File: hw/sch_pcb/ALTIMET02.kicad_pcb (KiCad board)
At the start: 2 copper layers, 40.1 x 19.8 mm, 14 parts, among them IC1 MS561101BA03-50, J2 HEADER_2x03, J3 HEADER_2x05_PARALLEL

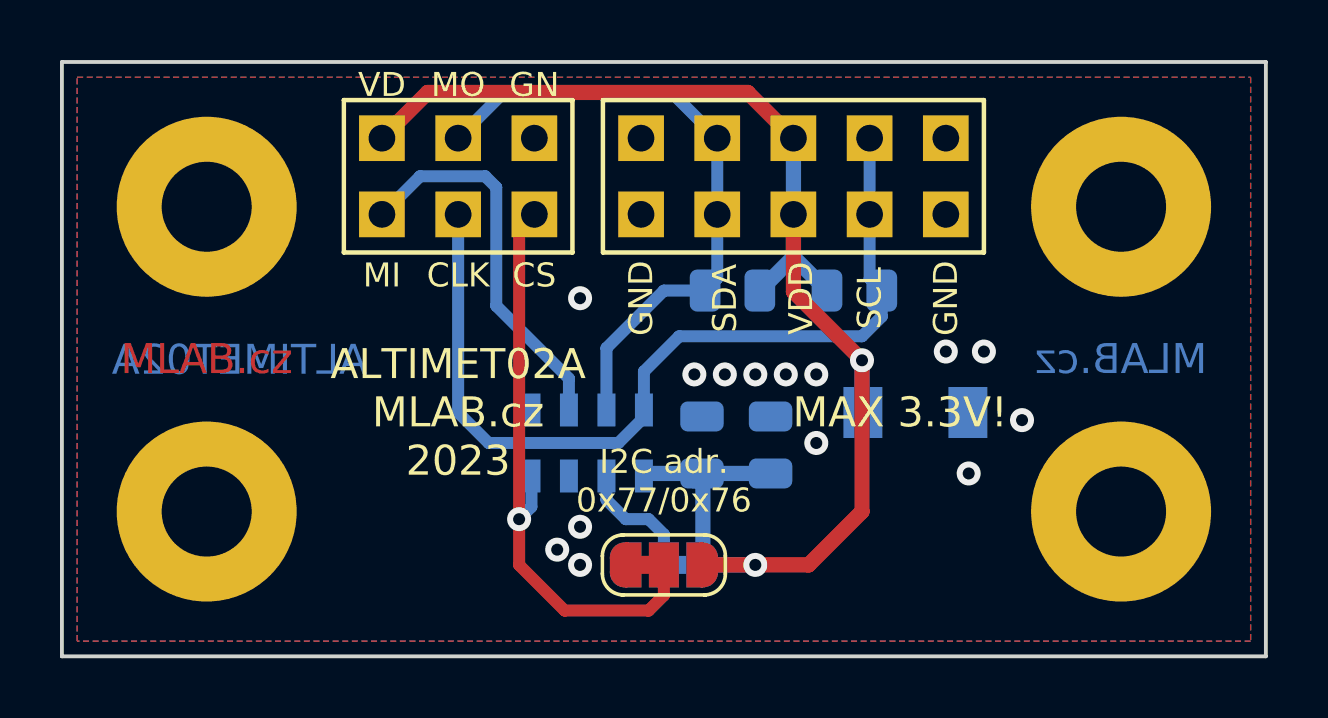
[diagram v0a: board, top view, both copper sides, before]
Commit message: power connector added, SPI and I2C connectors modified, default I2C adrress changed
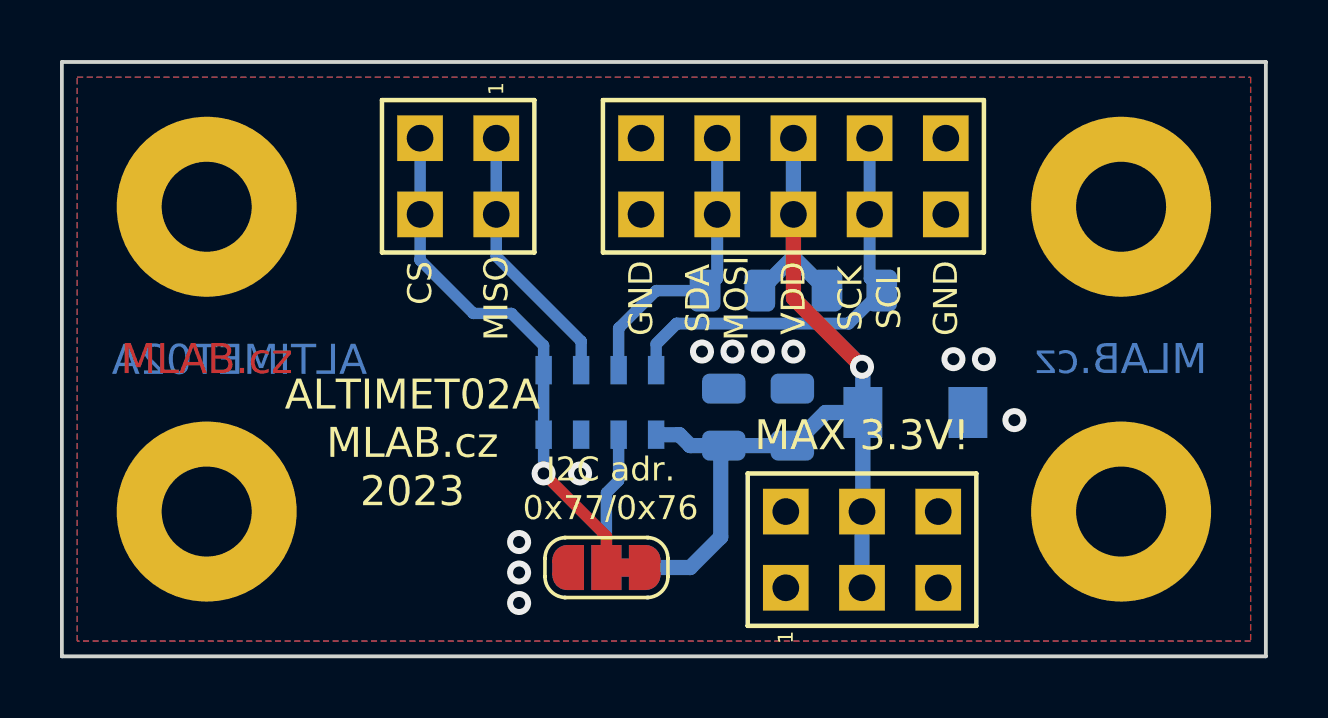
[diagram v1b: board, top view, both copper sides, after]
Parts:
- removed IC1: MS561101BA03-50, KiCad:MS561101BA03-50
- added J1: HEADER_2x02_PARALLEL, Mlab_Pin_Headers:Straight_2x02, F.Cu at (125.2, 100.6)
- added U1: MS5611-01BA, Package_LGA:LGA-8_3x5mm_P1.25mm, B.Cu at (129.9, 108.1)
- J2: value HEADER_2x03 -> HEADER_2x03_PARALLEL
- R1, R2: value DNF -> 5k
- moved J2 18.3 mm to (138.7, 113.0)
- moved JP1 1.92 mm to (130.2, 113.6)
- moved JP3 1.92 mm to (130.2, 113.6), turned to 180 degrees
- moved C1 1.18 mm to (134.1, 108.6)
- moved C2 1.18 mm to (136.4, 108.6)
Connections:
- J2 pad 1: MISO -> GND
- J2 pad 2: VDD -> GND
- J2 pad 3: SCLK -> VDD
- J2 pad 4: MOSI/SDA -> VDD
- J2 pad 5: CS/A -> GND
- JP3 pad 1: GND -> VDD
- JP3 pad 3: VDD -> GND
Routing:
- net VDD: track 50.4 -> 34.8 mm, vias 2 -> 1
- net SCLK: track 29.9 -> 14.4 mm
- net MOSI/SDA: track 21.3 -> 10.0 mm
- net MISO: track 13.4 -> 8.91 mm
- net CS/A: track 20.2 -> 17.6 mm
- net GND: vias 14 -> 11
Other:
- board text added: "MISO"
- board text added: "SCK SCL"
- board text added: "SDA MOSI"
- board text removed: "CLK"
- board text removed: "GN"
- board text removed: "MI"
- board text removed: "MO"
- board text removed: "SCL"
- board text removed: "SDA"
- board text removed: "VD"

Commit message: minor changes in layout, change diode
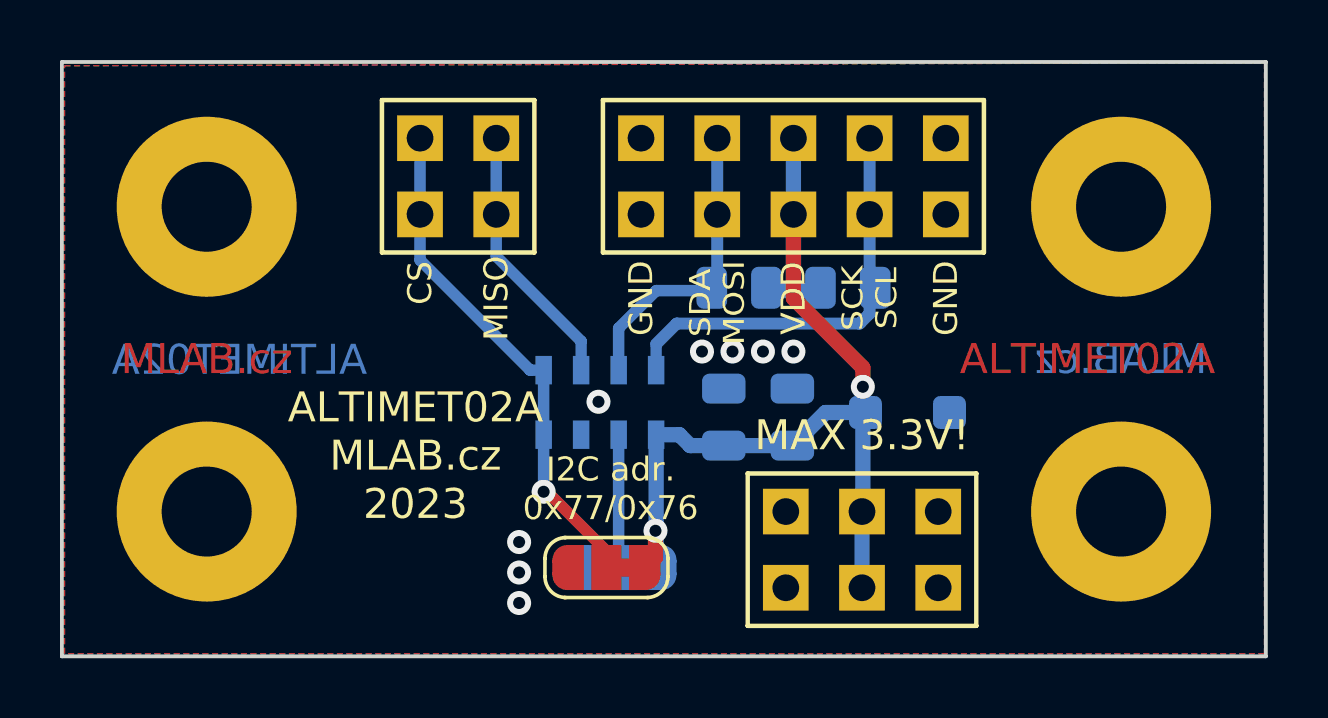
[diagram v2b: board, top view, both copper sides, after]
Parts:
- D1: value BZV55C3V6 -> BZT52H-C3V6,115; footprint Mlab_D:Diode-MiniMELF_Standard -> Diode_SMD:D_SOD-123F
- moved JP1 0.53 mm to (130.7, 113.6)
- moved D1 0.26 mm to (140.2, 108.5)
- moved R2 0.24 mm to (134.6, 104.3)
- moved R1 0.24 mm to (138.2, 104.3)
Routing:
- net VDD: vias 1 -> 2
- net GND: vias 11 -> 8

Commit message: add fiducial
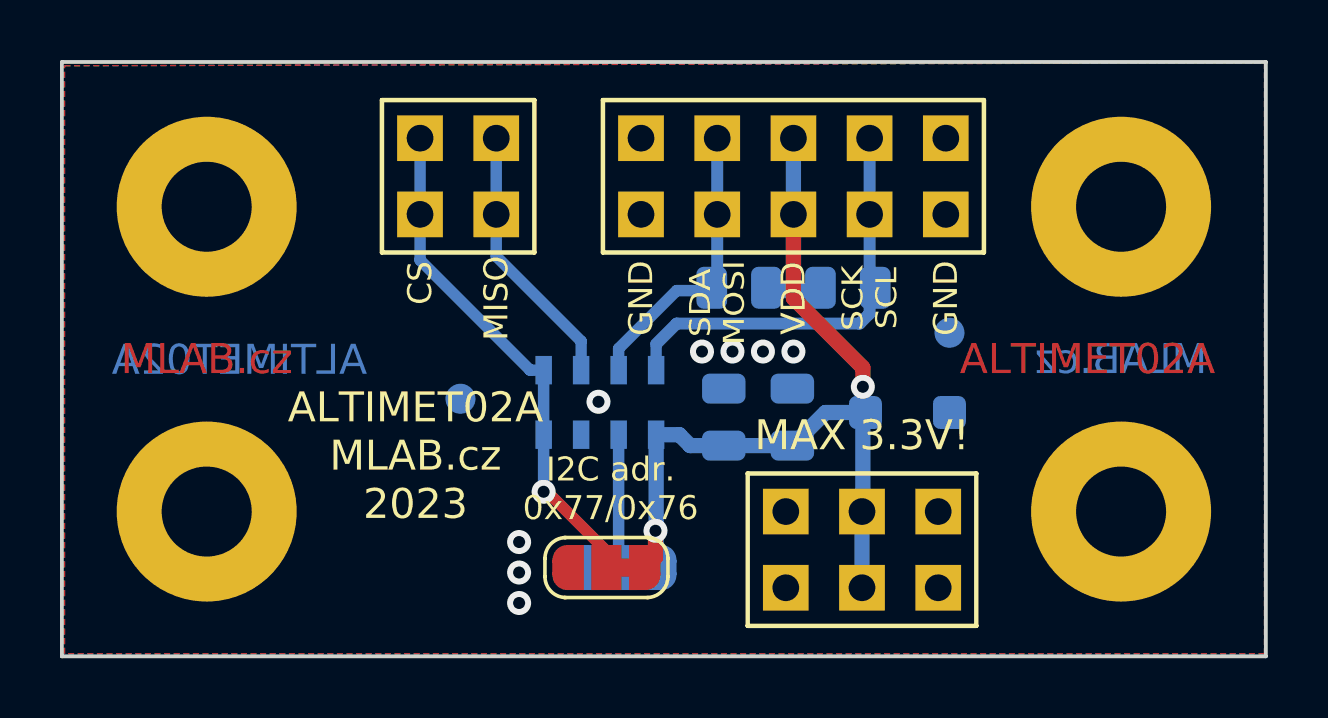
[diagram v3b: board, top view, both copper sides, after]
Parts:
- added FID1: Fiducial, Fiducial:Fiducial_1mm_Mask2mm, B.Cu at (141.6, 105.8)
- added FID2: Fiducial, Fiducial:Fiducial_1mm_Mask2mm, B.Cu at (125.3, 108.0)
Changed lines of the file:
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@@
     )
+  )
+  (footprint "Fiducial:Fiducial_1mm_Mask2mm" (layer "B.Cu")
+    (at 125.3 108 180)
+    (descr "Circular Fiducial, 1mm bare copper, 2mm soldermask opening (Level A)")
+    (tags "fiducial")
+    (property "Sheetfile" "ALTIMET02.kicad_sch")
+    (property "Sheetname" "")
+    (property "ki_description" "Fiducial Marker")
+    (property "ki_keywords" "fiducial marker")
+    (attr smd)
+    (fp_text reference "FID2" (at 0 2) (layer "B.SilkS") hide
+        (effects (font (size 1 1) (thickness 0.15)) (justify mirror))
+    )
+    (fp_text value "Fiducial" (at 0 -2) (layer "B.Fab")
+        (effects (font (size 1 1) (thickness 0.15)) (justify mirror))
+    )
+    (fp_text user "${REFERENCE}" (at 0 0) (layer "B.Fab")
+        (effects (font (size 0.4 0.4) (thickness 0.06)) (justify mirror))
+    )
+    (fp_circle (center 0 0) (end 1.25 0)
+      (stroke (width 0.05) (type solid)) (fill none) (layer "B.CrtYd"))
+    (fp_circle (center 0 0) (end 1 0)
+      (stroke (width 0.1) (type solid)) (fill none) (layer "B.Fab"))
+    (pad "" smd circle (at 0 0 180) (size 1 1) (layers "B.Cu" "B.Mask")
+      (solder_mask_margin 0.5) (clearance 0.5))
   )
   (footprint "Resistor_SMD:R_0805_2012Metric" (layer "B.Cu")
@@
       (rotate (xyz 0 0 0))
     )
+  )
+  (footprint "Fiducial:Fiducial_1mm_Mask2mm" (layer "B.Cu")
+    (at 141.6 105.8 180)
+    (descr "Circular Fiducial, 1mm bare copper, 2mm soldermask opening (Level A)")
+    (tags "fiducial")
+    (property "Sheetfile" "ALTIMET02.kicad_sch")
+    (property "Sheetname" "")
+    (property "ki_description" "Fiducial Marker")
+    (property "ki_keywords" "fiducial marker")
+    (attr smd)
+    (fp_text reference "FID1" (at 0 2) (layer "B.SilkS") hide
+        (effects (font (size 1 1) (thickness 0.15)) (justify mirror))
+    )
+    (fp_text value "Fiducial" (at 0 -2) (layer "B.Fab")
+        (effects (font (size 1 1) (thickness 0.15)) (justify mirror))
+    )
+    (fp_text user "${REFERENCE}" (at 0 0) (layer "B.Fab")
+        (effects (font (size 0.4 0.4) (thickness 0.06)) (justify mirror))
+    )
+    (fp_circle (center 0 0) (end 1.25 0)
+      (stroke (width 0.05) (type solid)) (fill none) (layer "B.CrtYd"))
+    (fp_circle (center 0 0) (end 1 0)
+      (stroke (width 0.1) (type solid)) (fill none) (layer "B.Fab"))
+    (pad "" smd circle (at 0 0 180) (size 1 1) (layers "B.Cu" "B.Mask")
+      (solder_mask_margin 0.5) (clearance 0.5))
   )
   (footprint "Capacitor_SMD:C_0805_2012Metric" (layer "B.Cu")
@@
   (segment (start 131.8214 112.3786) (end 131.8 112.4) (width 0.508) (layer "B.Cu") (net 1))
   (segment (start 134.0766 109.562) (end 133.975 109.6636) (width 0.508) (layer "B.Cu") (net 1))
-  (segment (start 130.5714 105.6486) (end 131.826 104.394) (width 0.381) (layer "B.Cu") (net 2))
   (segment (start 133.858 103.9895) (end 133.4535 104.394) (width 0.4) (layer "B.Cu") (net 2))
+  (segment (start 132.506 104.394) (end 133.4535 104.394) (width 0.381) (layer "B.Cu") (net 2))
   (segment (start 133.858 101.854) (end 133.858 103.9895) (width 0.4) (layer "B.Cu") (net 2))
   (segment (start 133.858 99.314) (end 133.858 101.854) (width 0.4) (layer "B.Cu") (net 2))
-  (segment (start 130.5714 107.0474) (end 130.5714 105.6486) (width 0.381) (layer "B.Cu") (net 2))
-  (segment (start 131.826 104.394) (end 133.4535 104.394) (width 0.381) (layer "B.Cu") (net 2))
+  (segment (start 130.5714 107.0474) (end 130.5714 106.3286) (width 0.381) (layer "B.Cu") (net 2))
+  (segment (start 130.5714 106.3286) (end 132.506 104.394) (width 0.381) (layer "B.Cu") (net 2))
   (segment (start 126.492 101.854) (end 126.492 99.314) (width 0.381) (layer "B.Cu") (net 3))
   (segment (start 126.492 103.251) (end 126.492 101.854) (width 0.381) (layer "B.Cu") (net 3))

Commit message: Fix sharp trace. Improve silkscreen.
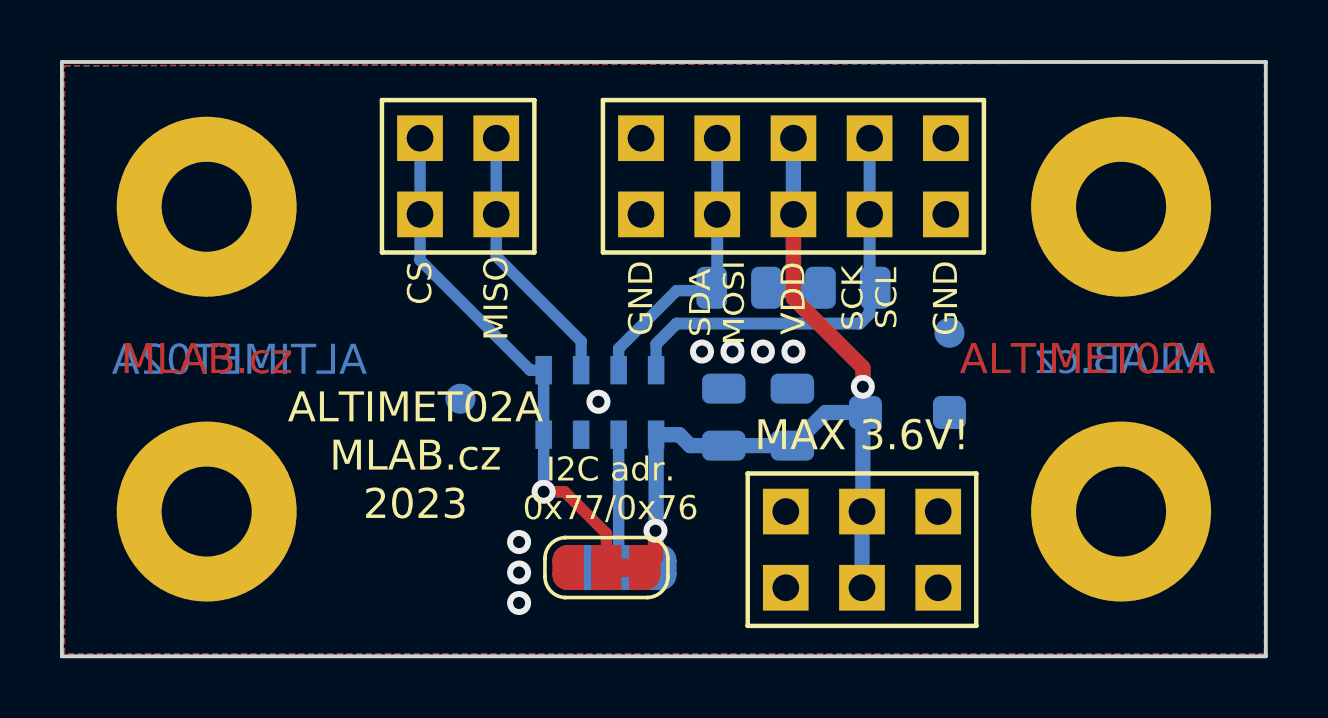
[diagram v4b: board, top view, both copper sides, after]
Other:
- board text added: "MAX 3.6V!"
- board text removed: "MAX 3.3V!"
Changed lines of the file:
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@@
   )
   (paper "A4")
+  (title_block
+    (comment 2 "Digital altimeter  \\nand barometer sensor\\nwith I²C or SPI interface")
+  )
   (layers
     (0 "F.Cu" signal)
@@
     (effects (font (size 0.8 0.8) (thickness 0.15)))
   )
-  (gr_text "MAX 3.3V!" (at 138.684 109.22) (layer "F.SilkS")
+  (gr_text "MAX 3.6V!" (at 138.684 109.22) (layer "F.SilkS")
     (effects (font (size 1 1) (thickness 0.15)))
   )
@@
   (segment (start 129.3214 106.0804) (end 126.492 103.251) (width 0.381) (layer "B.Cu") (net 3))
   (segment (start 129.3214 107.0474) (end 129.3214 106.0804) (width 0.381) (layer "B.Cu") (net 3))
-  (segment (start 130.165 113.07375) (end 130.165 113.626) (width 0.381) (layer "F.Cu") (net 4))
-  (segment (start 128.19125 111.1) (end 130.165 113.07375) (width 0.381) (layer "F.Cu") (net 4))
-  (segment (start 128.0714 111.1) (end 128.19125 111.1) (width 0.381) (layer "F.Cu") (net 4))
+  (segment (start 130.165 112.495) (end 130.165 113.626) (width 0.381) (layer "F.Cu") (net 4))
+  (segment (start 128.0714 111.1) (end 128.77 111.1) (width 0.381) (layer "F.Cu") (net 4))
+  (segment (start 128.77 111.1) (end 130.165 112.495) (width 0.381) (layer "F.Cu") (net 4))
   (via (at 128.0714 111.1) (size 0.8) (drill 0.4) (layers "F.Cu" "B.Cu") (net 4))
   (segment (start 128.0714 111.1) (end 128.0714 109.1974) (width 0.381) (layer "B.Cu") (net 4))

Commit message: add ustid
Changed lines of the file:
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@@
   (via (at 138.712 107.6) (size 0.8) (drill 0.4) (layers "F.Cu" "B.Cu") (net 1))
   (segment (start 136.398 101.854) (end 136.4 101.856) (width 0.508) (layer "B.Cu") (net 1))
-  (segment (start 137.4666 108.458) (end 136.3626 109.562) (width 0.508) (layer "B.Cu") (net 1))
   (segment (start 131.8214 112.4214) (end 131.8214 113.4474) (width 0.508) (layer "B.Cu") (net 1))
   (segment (start 136.4 101.856) (end 136.4 104.392) (width 0.508) (layer "B.Cu") (net 1))
   (segment (start 138.684 108.43) (end 138.712 108.458) (width 0.508) (layer "B.Cu") (net 1))
+  (segment (start 138.712 109.562) (end 136.3626 109.562) (width 0.508) (layer "B.Cu") (net 1))
+  (segment (start 131.824 109.2) (end 131.8214 109.1974) (width 0.508) (layer "B.Cu") (net 1))
   (segment (start 136.398 104.394) (end 135.2785 104.394) (width 0.508) (layer "B.Cu") (net 1))
+  (segment (start 133.7146 109.2) (end 131.824 109.2) (width 0.508) (layer "B.Cu") (net 1))
   (segment (start 136.4 104.392) (end 136.398 104.394) (width 0.508) (layer "B.Cu") (net 1))
   (segment (start 138.712 107.6) (end 138.712 108.458) (width 0.508) (layer "B.Cu") (net 1))
@@
   (segment (start 138.712 111.732) (end 138.684 111.76) (width 0.508) (layer "B.Cu") (net 1))
   (segment (start 132 113.626) (end 132 113.8) (width 0.2) (layer "B.Cu") (net 1))
-  (segment (start 134.0766 109.562) (end 132.959 109.562) (width 0.508) (layer "B.Cu") (net 1))
   (segment (start 138.684 111.76) (end 138.684 114.3) (width 0.508) (layer "B.Cu") (net 1))
-  (segment (start 132.5944 109.1974) (end 131.8214 109.1974) (width 0.508) (layer "B.Cu") (net 1))
-  (segment (start 132.959 109.562) (end 132.5944 109.1974) (width 0.508) (layer "B.Cu") (net 1))
   (segment (start 134.1066 109.592) (end 134.0766 109.562) (width 0.508) (layer "B.Cu") (net 1))
   (segment (start 138.712 108.458) (end 138.712 111.732) (width 0.508) (layer "B.Cu") (net 1))
-  (segment (start 138.712 108.458) (end 137.4666 108.458) (width 0.508) (layer "B.Cu") (net 1))
   (segment (start 131.8214 113.4474) (end 132 113.626) (width 0.508) (layer "B.Cu") (net 1))
   (segment (start 131.8 112.4) (end 131.8214 112.4214) (width 0.508) (layer "B.Cu") (net 1))
@@
   (segment (start 131.8214 112.3786) (end 131.8 112.4) (width 0.508) (layer "B.Cu") (net 1))
   (segment (start 134.0766 109.562) (end 133.975 109.6636) (width 0.508) (layer "B.Cu") (net 1))
+  (segment (start 134.0766 109.562) (end 133.7146 109.2) (width 0.508) (layer "B.Cu") (net 1))
   (segment (start 133.858 103.9895) (end 133.4535 104.394) (width 0.4) (layer "B.Cu") (net 2))
   (segment (start 132.506 104.394) (end 133.4535 104.394) (width 0.381) (layer "B.Cu") (net 2))
